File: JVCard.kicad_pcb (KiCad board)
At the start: 2 copper layers, 170 x 130 mm, 75 parts, among them J6 Conn_02x25_Odd_Even, Q1 mmbt3904, Q2 mmbt3904, Q3 mmbt3904, Q4 mmbt3904, Q5 mmbt3904, Q6 mmbt3904, U4 SCART_CONN, U5 MET1117A50B3G

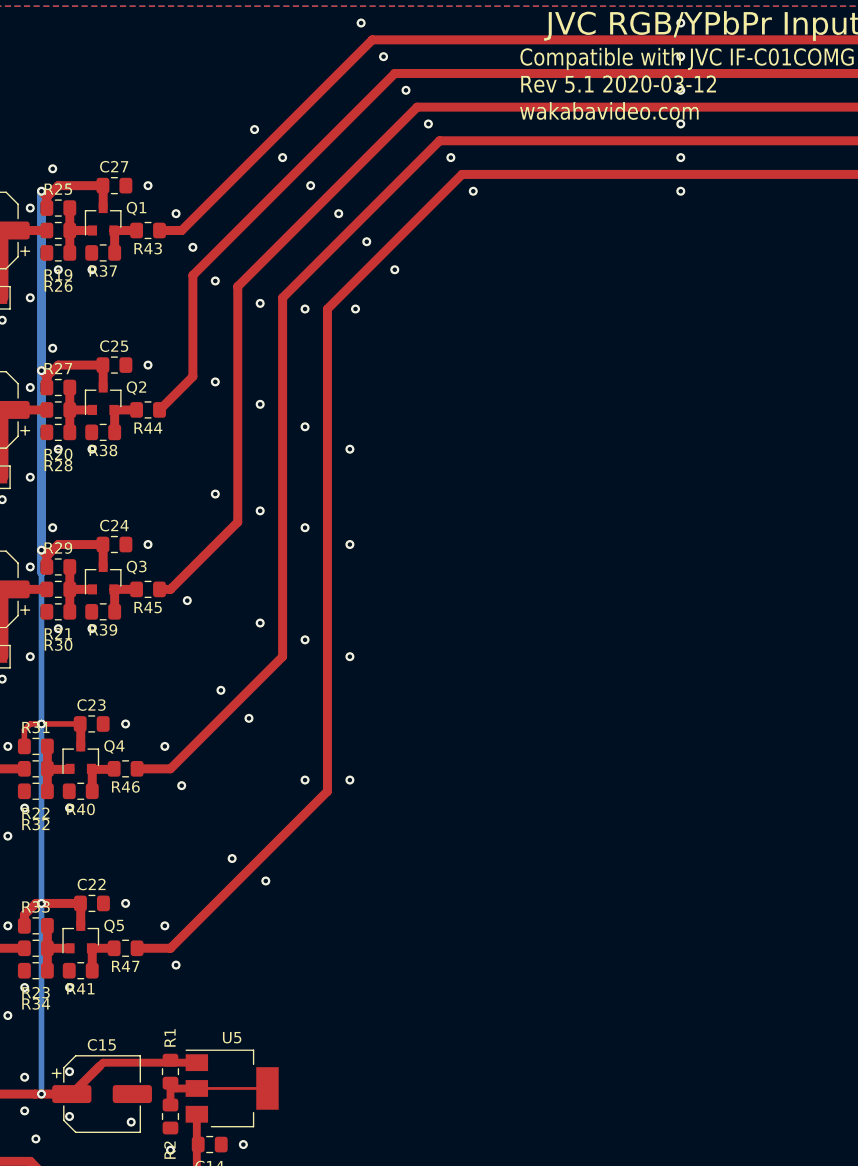
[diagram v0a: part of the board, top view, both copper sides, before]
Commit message: fixed regularot pinout whoops
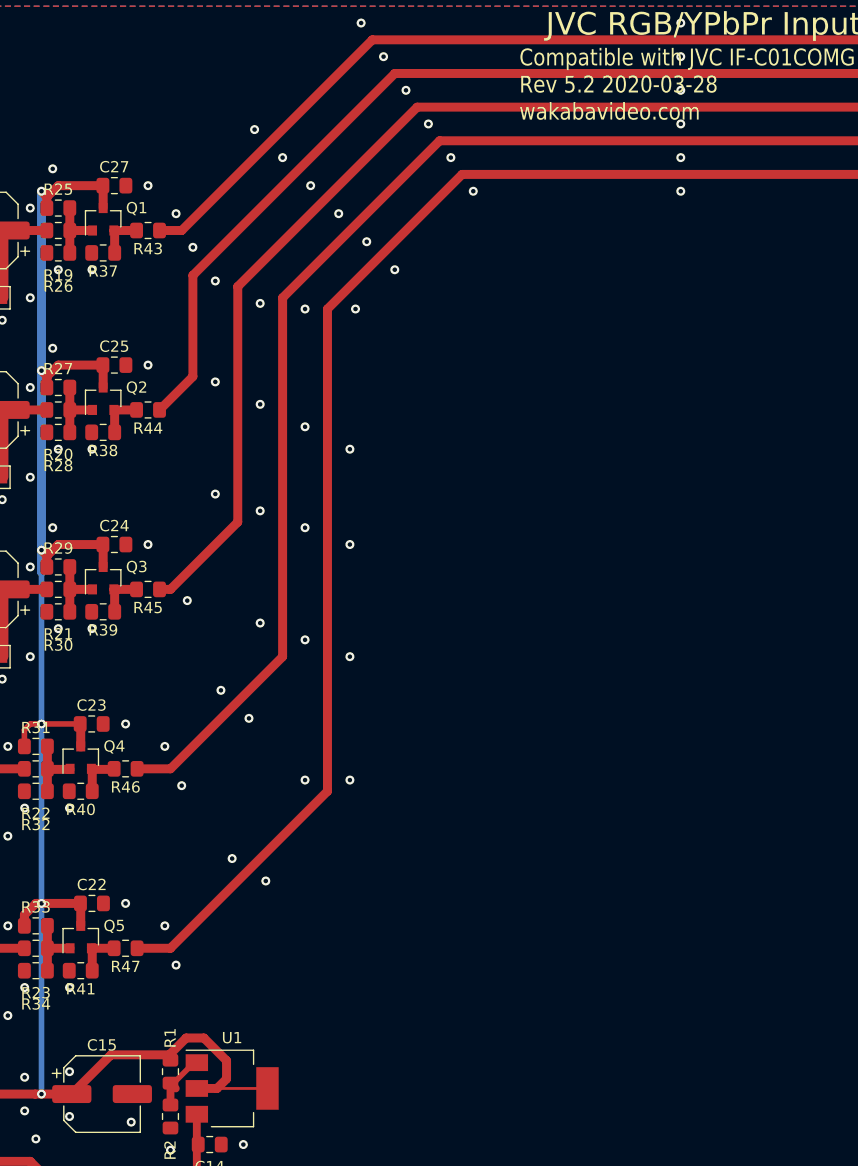
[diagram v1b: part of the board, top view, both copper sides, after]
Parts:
- removed U5: MET1117A50B3G, Package_TO_SOT_SMD:SOT-223-3_TabPin2
- added U1: AMS1117-5.0, Package_TO_SOT_SMD:SOT-223-3_TabPin2, F.Cu at (-4.50, 107.5)
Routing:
- net +12V: track 165.8 -> 181.1 mm
- net Net-(R1-Pad2): track 10.8 -> 5.73 mm
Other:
- board text added: "Compatible with JVC IF-C01COMG / Panasonic BT-YA702 Rev 5.2 2020-03-28 wakabavideo.com"
- board text removed: "Compatible with JVC IF-C01COMG / Panasonic BT-YA702 Rev 5.1 2020-03-12 wakabavideo.com"

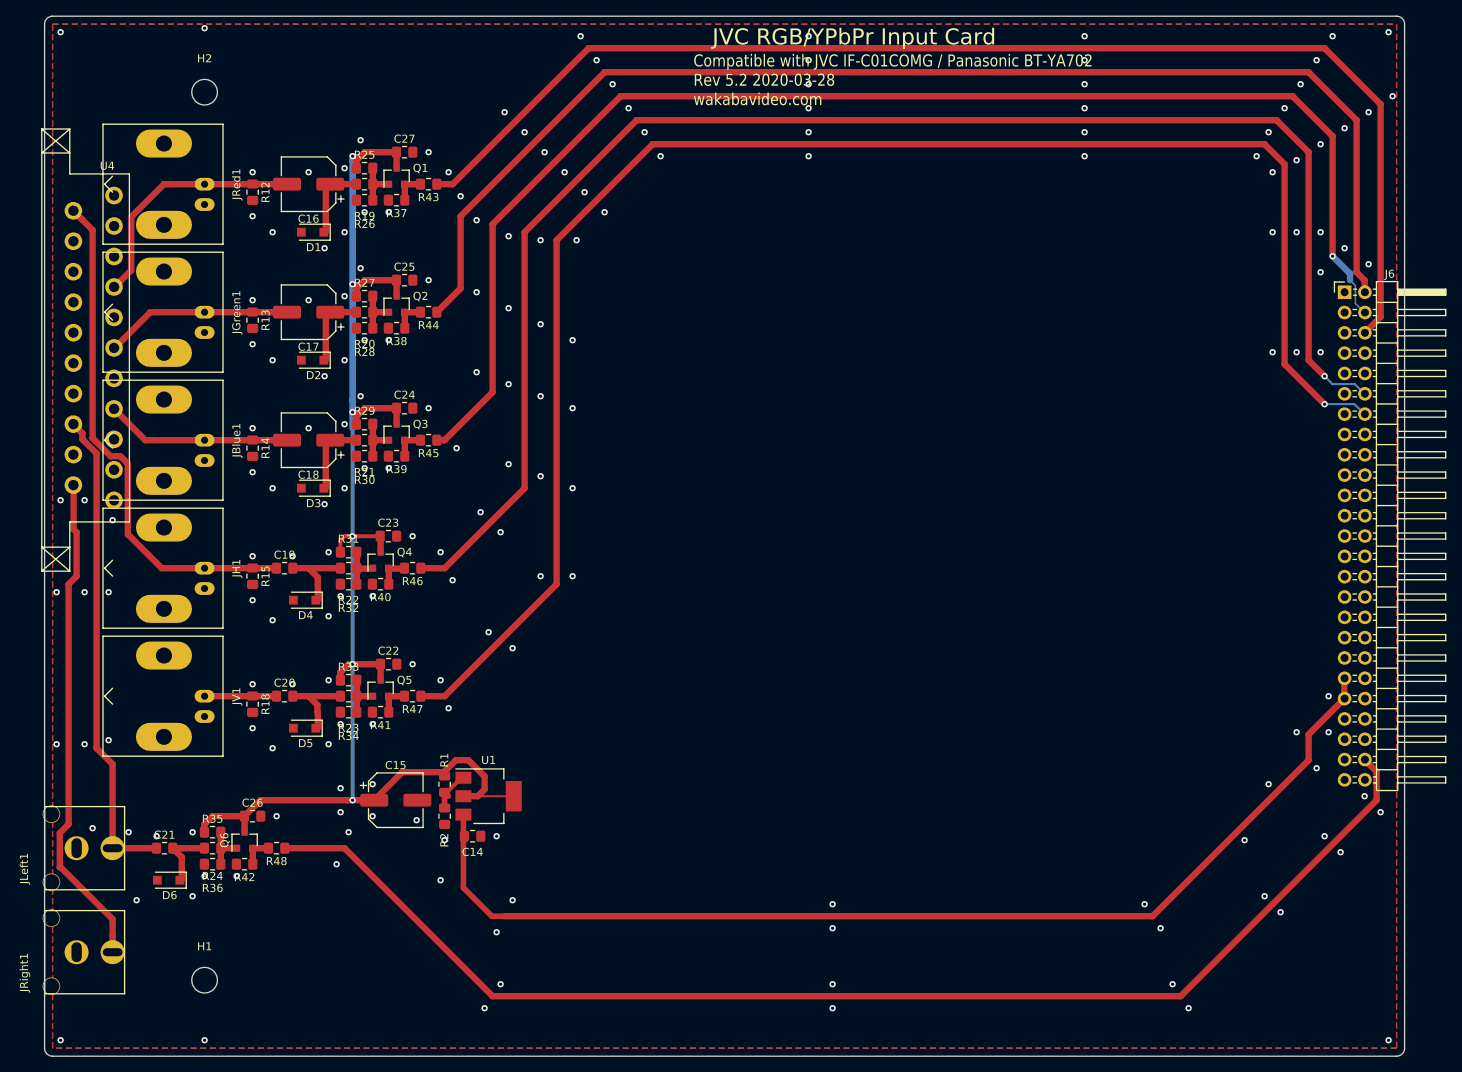
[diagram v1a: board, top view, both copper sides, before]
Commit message: add rear panel
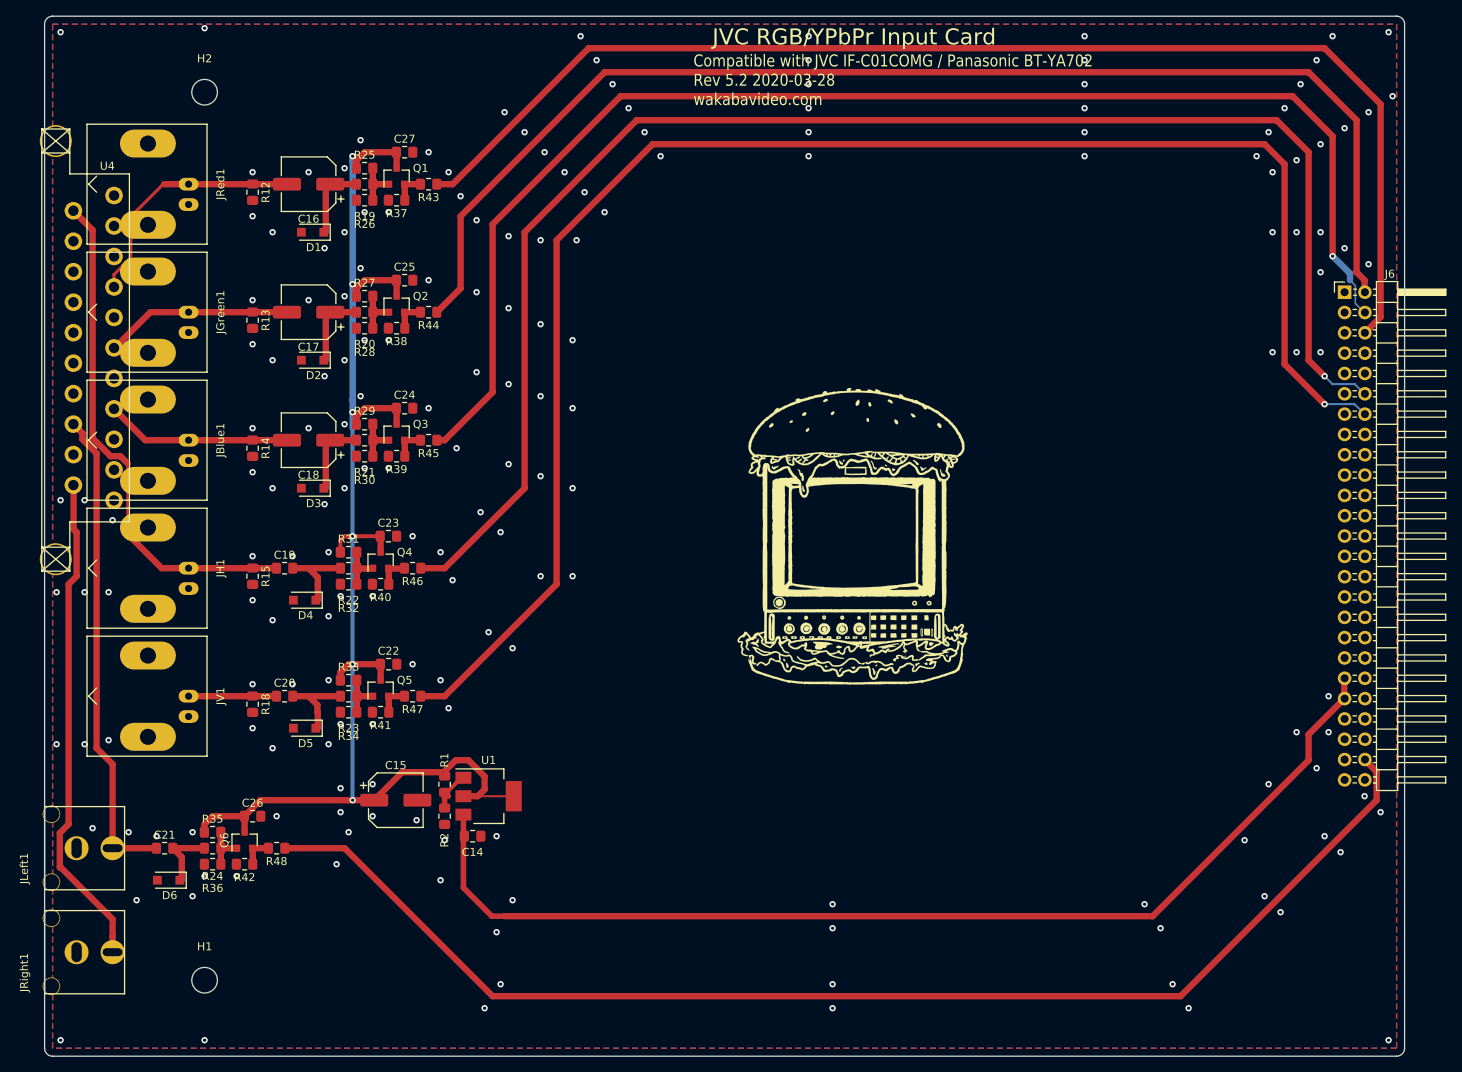
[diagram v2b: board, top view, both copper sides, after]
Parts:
- added FID101: Borgar, videobits:borgar, F.Cu at (41.0, 75.0)
- R2: value 4k8 -> 1k
- moved JBlue1 2.00 mm to (-42.0, 63.0)
- moved JGreen1 2.00 mm to (-42.0, 47.0)
- moved JH1 2.00 mm to (-42.0, 79.0)
- moved JRed1 2.00 mm to (-42.0, 31.0)
- moved JV1 2.00 mm to (-42.0, 95.0)
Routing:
- net /Ri: track 30.8 -> 32.9 mm
- net /Vi: track 8.98 -> 11.0 mm

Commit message: 4 way panelised
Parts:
- JBlue1, JGreen1, JH1, JRed1, JV1: footprint Connector_Coaxial:BNC_Amphenol_B6252HB-NPP3G-50_Horizontal -> videobits:BNC_Amphenol_B6252HB-NPP3G-50_Horizontal_smallerpads
- moved FID101 22.4 mm to (19.0, 79.0)

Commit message: resync
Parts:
- removed FID101: Borgar, videobits:borgar
- added G***: LOGO, videobits:wakaba, F.Cu at (17.9, 14.4)
- added G***: LOGO, videobits:borgar, F.Cu at (48.6, 75.0)

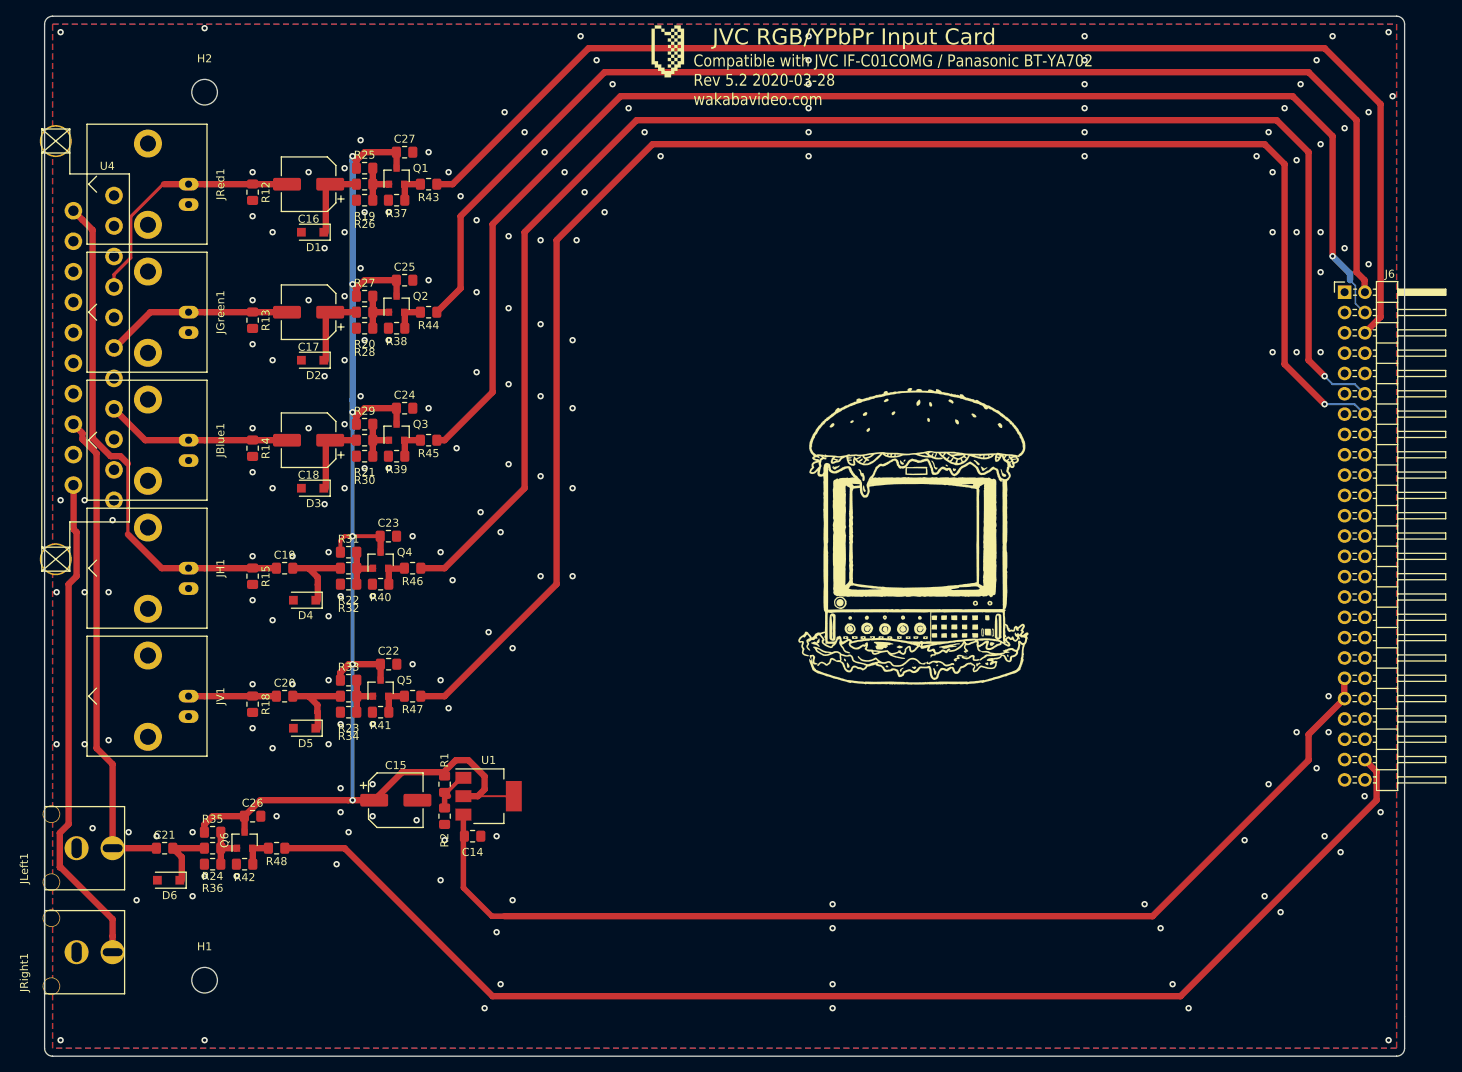
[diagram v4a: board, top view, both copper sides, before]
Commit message: updated kicad version, parts and fab file updates
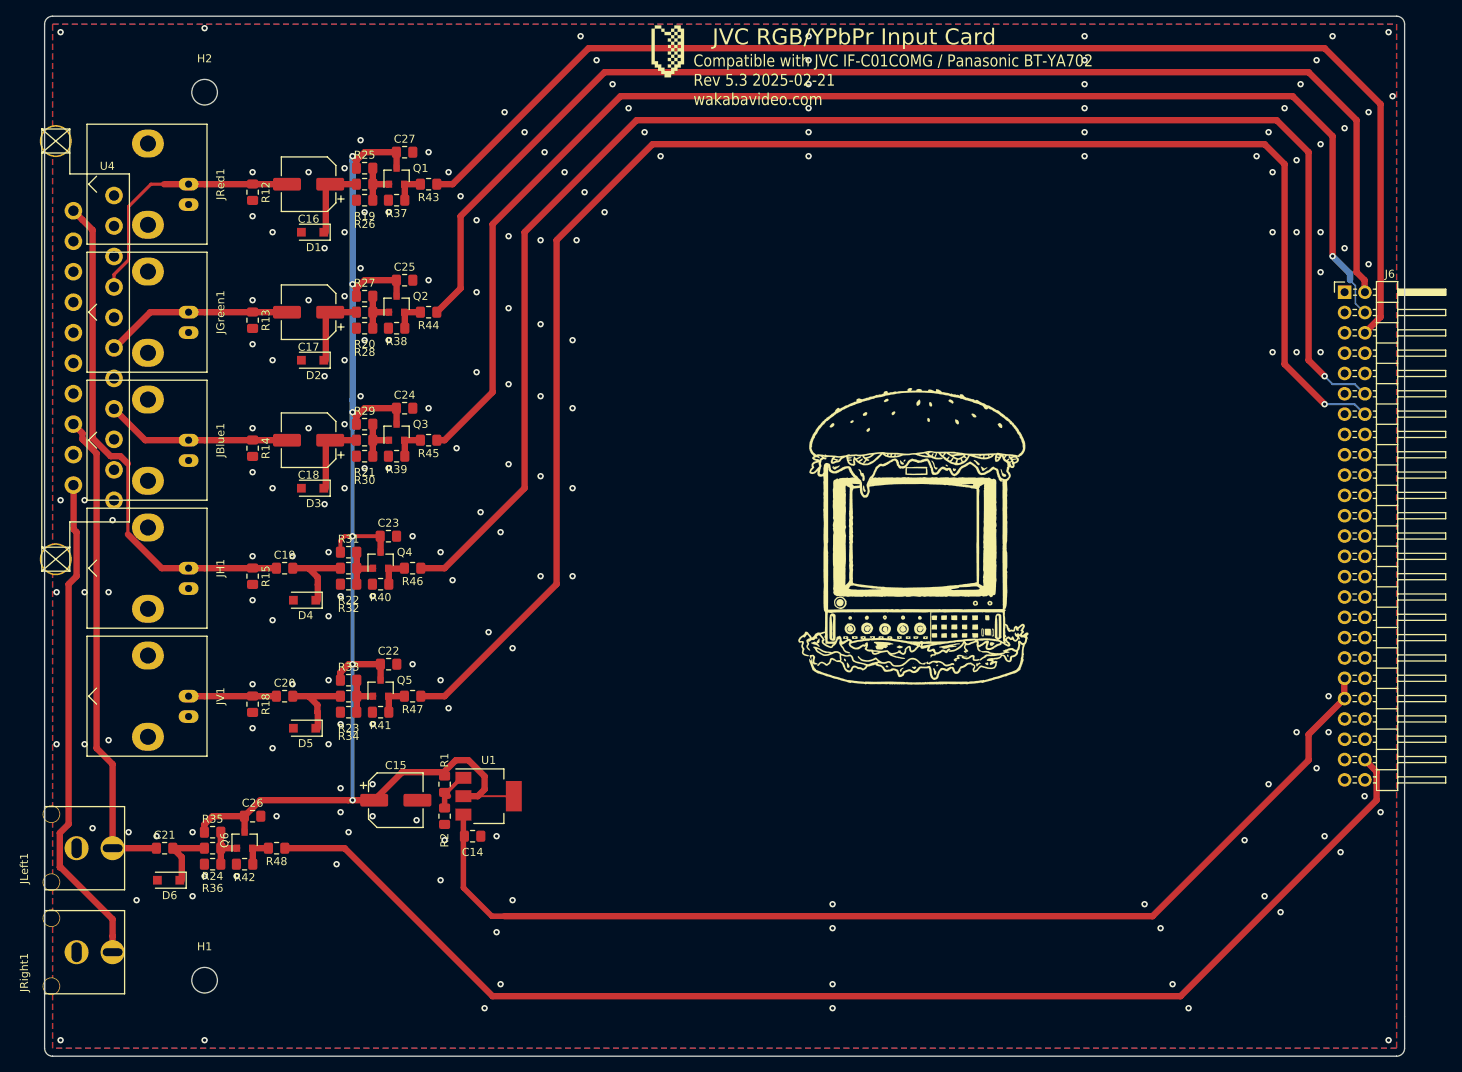
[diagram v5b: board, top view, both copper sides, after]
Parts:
- JBlue1, JGreen1, JH1, JRed1, JV1: footprint videobits:BNC_Amphenol_B6252HB-NPP3G-50_Horizontal_smallerpads -> Connector_Coaxial:BNC_Amphenol_B6252HB-NPP3G-50_Horizontal-x4mmhole
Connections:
- J6 pad 10: Net-(J6-Pad10) -> unconnected-(J6-Pin_10-Pad10)
- J6 pad 15: Net-(J6-Pad15) -> unconnected-(J6-Pin_15-Pad15)
- J6 pad 16: Net-(J6-Pad16) -> unconnected-(J6-Pin_16-Pad16)
- J6 pad 17: Net-(J6-Pad17) -> unconnected-(J6-Pin_17-Pad17)
- J6 pad 18: Net-(J6-Pad18) -> unconnected-(J6-Pin_18-Pad18)
- J6 pad 20: Net-(J6-Pad20) -> unconnected-(J6-Pin_20-Pad20)
- J6 pad 22: Net-(J6-Pad22) -> unconnected-(J6-Pin_22-Pad22)
- J6 pad 23: Net-(J6-Pad23) -> unconnected-(J6-Pin_23-Pad23)
- J6 pad 24: Net-(J6-Pad24) -> unconnected-(J6-Pin_24-Pad24)
- J6 pad 26: Net-(J6-Pad26) -> unconnected-(J6-Pin_26-Pad26)
- J6 pad 27: Net-(J6-Pad27) -> unconnected-(J6-Pin_27-Pad27)
- J6 pad 28: Net-(J6-Pad28) -> unconnected-(J6-Pin_28-Pad28)
- J6 pad 29: Net-(J6-Pad29) -> unconnected-(J6-Pin_29-Pad29)
- J6 pad 30: Net-(J6-Pad30) -> unconnected-(J6-Pin_30-Pad30)
- J6 pad 32: Net-(J6-Pad32) -> unconnected-(J6-Pin_32-Pad32)
- J6 pad 33: Net-(J6-Pad33) -> unconnected-(J6-Pin_33-Pad33)
- J6 pad 34: Net-(J6-Pad34) -> unconnected-(J6-Pin_34-Pad34)
- J6 pad 35: Net-(J6-Pad35) -> unconnected-(J6-Pin_35-Pad35)
- J6 pad 36: Net-(J6-Pad36) -> unconnected-(J6-Pin_36-Pad36)
- J6 pad 37: Net-(J6-Pad37) -> unconnected-(J6-Pin_37-Pad37)
- J6 pad 38: Net-(J6-Pad38) -> unconnected-(J6-Pin_38-Pad38)
- J6 pad 40: Net-(J6-Pad40) -> unconnected-(J6-Pin_40-Pad40)
- J6 pad 42: Net-(J6-Pad42) -> unconnected-(J6-Pin_42-Pad42)
- J6 pad 43: Net-(J6-Pad43) -> unconnected-(J6-Pin_43-Pad43)
- J6 pad 44: Net-(J6-Pad44) -> unconnected-(J6-Pin_44-Pad44)
- J6 pad 45: Net-(J6-Pad45) -> unconnected-(J6-Pin_45-Pad45)
- J6 pad 46: Net-(J6-Pad46) -> unconnected-(J6-Pin_46-Pad46)
- J6 pad 8: Net-(J6-Pad8) -> unconnected-(J6-Pin_8-Pad8)
- J6 pad 9: Net-(J6-Pad9) -> unconnected-(J6-Pin_9-Pad9)
- U4 pad 1: Net-(U4-Pad1) -> unconnected-(U4-AUD_OUT_R-Pad1)
- U4 pad 10: Net-(U4-Pad10) -> unconnected-(U4-IOCTRL-Pad10)
- U4 pad 12: Net-(U4-Pad12) -> unconnected-(U4-RSV-Pad12)
- U4 pad 16: Net-(U4-Pad16) -> unconnected-(U4-RGB_STAT-Pad16)
- U4 pad 19: Net-(U4-Pad19) -> unconnected-(U4-SYNC_OUT-Pad19)
- U4 pad 3: Net-(U4-Pad3) -> unconnected-(U4-AUD_OUT_L-Pad3)
- U4 pad 8: Net-(U4-Pad8) -> unconnected-(U4-VID_STAT-Pad8)
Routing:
- net /Ri: track 32.9 -> 33.8 mm
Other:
- net class Default removed
- board text added: "Compatible with JVC IF-C01COMG / Panasonic BT-YA702 Rev 5.3 2025-02-21 wakabavideo.com"
- board text removed: "Compatible with JVC IF-C01COMG / Panasonic BT-YA702 Rev 5.2 2020-03-28 wakabavideo.com"
